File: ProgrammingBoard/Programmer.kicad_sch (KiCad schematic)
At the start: 2 parts, among them J5 Conn_01x20, J6 Conn_01x20

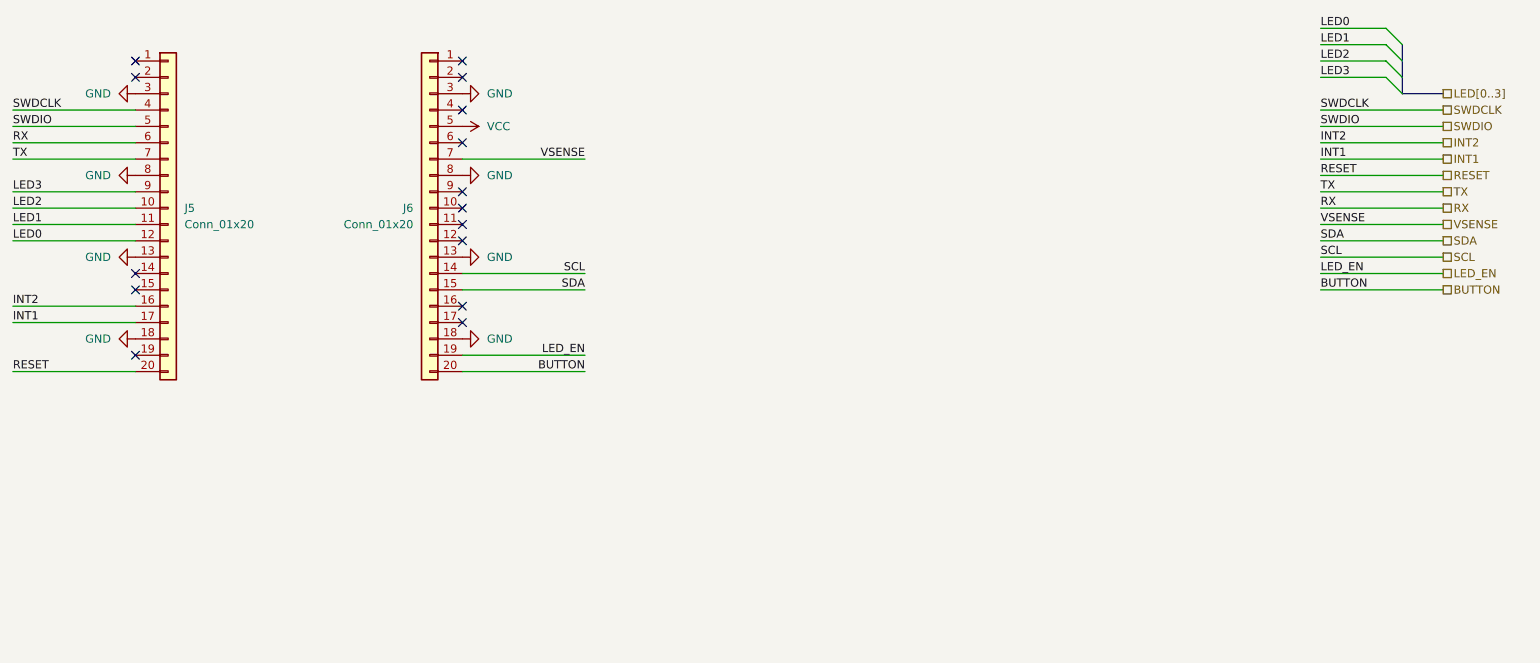
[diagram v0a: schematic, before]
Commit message: Remove LED driver
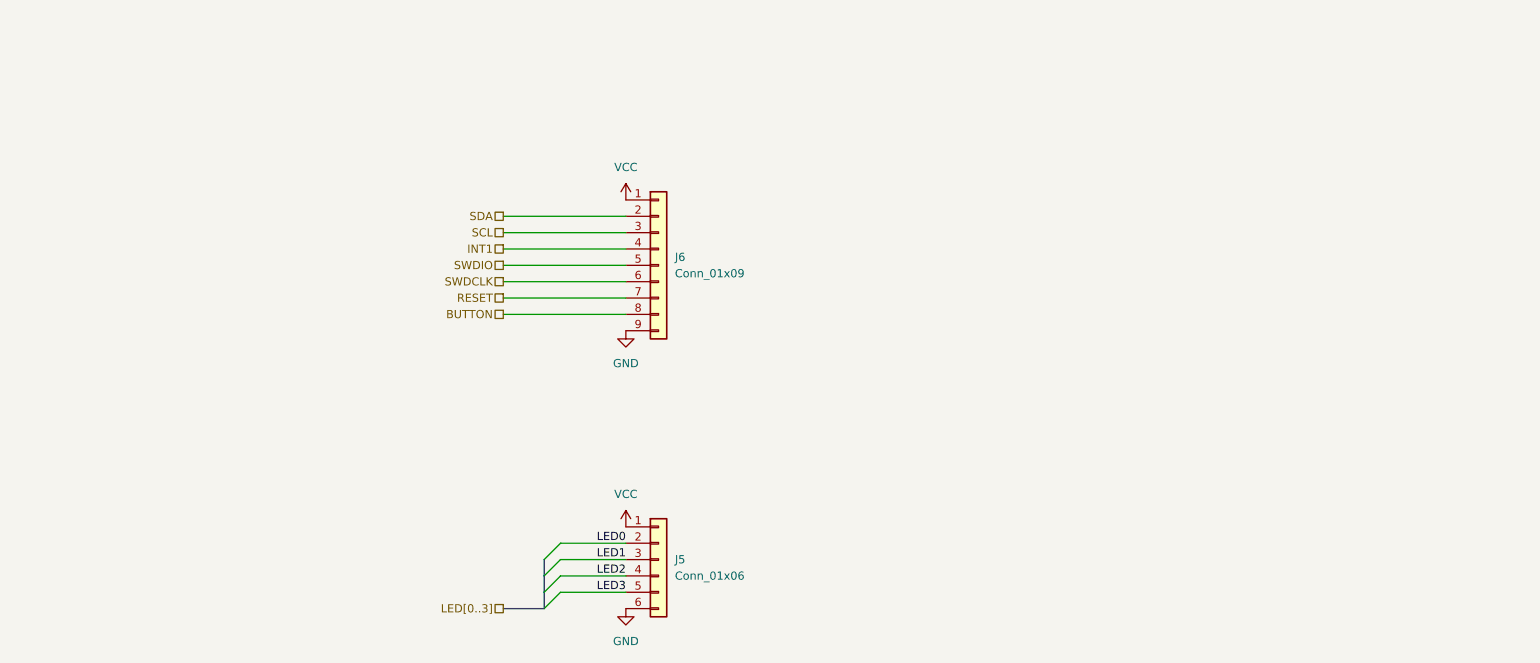
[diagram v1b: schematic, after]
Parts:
- removed J5, J6: Conn_01x20, Connector_PinSocket_2.54mm:PinSocket_1x20_P2.54mm_Vertical, symbol Connector_Generic:Conn_01x20
- added J5: Conn_01x06, Connector_PinHeader_2.54mm:PinHeader_1x06_P2.54mm_Vertical, symbol Connector_Generic:Conn_01x06
- added J6: Conn_01x09, Connector_PinHeader_2.54mm:PinHeader_1x09_P2.54mm_Vertical, symbol Connector_Generic:Conn_01x09
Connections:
- net BUTTON: now also J6.8 (Pin_8)
- net GND: now also J5.6 (Pin_6), J6.9 (Pin_9)
- net INT1: now also J6.4 (Pin_4)
- net LED0: now also J5.2 (Pin_2)
- net LED1: now also J5.3 (Pin_3)
- net LED2: now also J5.4 (Pin_4)
- net LED3: now also J5.5 (Pin_5)
- net RESET: now also J6.7 (Pin_7)
- net SCL: now also J6.3 (Pin_3)
- net SDA: now also J6.2 (Pin_2)
- net SWDCLK: now also J6.6 (Pin_6)
- net SWDIO: now also J6.5 (Pin_5)
- net VCC: now also J5.1 (Pin_1), J6.1 (Pin_1)
- no-connect marks 15 -> 0

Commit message: Change led matrix routing for sinking current through mcu, sourcing from battery
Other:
- title: (none) -> WordWatch - Programming Board
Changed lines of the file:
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@@
 (kicad_sch (version 20230121) (generator eeschema)
   (paper "A4")
+  (title_block
+    (title "WordWatch - Programming Board")
+    (date "2023-11-11")
+    (rev "1.0")
+  )
   (bus_entry (at 107.95 107.95) (size 2.54 -2.54)
     (stroke (width 0) (type default))
